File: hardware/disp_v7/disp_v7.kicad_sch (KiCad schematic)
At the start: 109 parts, among them J1 Conn_02x16_Odd_Even, Q1 2N7002, Q10 2N7002, Q11 2N7002, Q2 2N7002, Q3 2N7002, Q4 2N7002, Q5 2N7002, Q6 2N7002, Q7 2N7002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

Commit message: update version on disp to v7
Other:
- title: Disp V6 -> Disp

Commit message: main counter counting
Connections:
- net AUX_GPS_PPS: no longer names the net of J1.31 (Pin_31)
- net BOOT0: no longer names the net of R2.2
- net BOOT0: no longer J1.29 (Pin_29)
- net BOOT1: no longer names the net of J1.21 (Pin_21)
- net BOOT1: no longer R1.2
- net GPS_PPS: no longer names the net of J1.32 (Pin_32)
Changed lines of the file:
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@@
-    (effects (font (size 1.27 1.27)) (justify left bottom))
-  )
-  (label "BOOT0" (at 33.02 59.69 180) (fields_autoplaced)
-    (effects (font (size 1.27 1.27)) (justify right bottom))
-  )
-  (label "BOOT0" (at 171.45 25.4 0) (fields_autoplaced)
     (effects (font (size 1.27 1.27)) (justify left bottom))
   )
@@
     (effects (font (size 1.27 1.27)) (justify left bottom))
   )
-  (label "BOOT1" (at 171.45 36.83 0) (fields_autoplaced)
-    (effects (font (size 1.27 1.27)) (justify left bottom))
-  )
-  (label "BOOT1" (at 26.67 49.53 0) (fields_autoplaced)
-    (effects (font (size 1.27 1.27)) (justify left bottom))
-  )
   (label "ROW4" (at 26.67 36.83 0) (fields_autoplaced)
     (effects (font (size 1.27 1.27)) (justify left bottom))
@@
   (label "LEDH" (at 48.26 140.97 0) (fields_autoplaced)
     (effects (font (size 1.27 1.27)) (justify left bottom))
-  )
-  (label "AUX_GPS_PPS" (at 33.02 62.23 180) (fields_autoplaced)
-    (effects (font (size 1.27 1.27)) (justify right bottom))
   )
   (label "ROW6" (at 48.26 46.99 0) (fields_autoplaced)
@@
     (effects (font (size 1.27 1.27)) (justify left bottom))
   )
-  (label "GPS_PPS" (at 45.72 62.23 0) (fields_autoplaced)
-    (effects (font (size 1.27 1.27)) (justify left bottom))
-  )

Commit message: add switches
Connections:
- net ROW10: now reaches R2.2
- net ROW10: now also J1.29 (Pin_29)
- net ROW9: now reaches J1.21 (Pin_21)
- net ROW9: now also R1.2
- no-connect marks 0 -> 2
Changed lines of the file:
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@@
   (junction (at 88.9 148.59) (diameter 0) (color 0 0 0 0)
   )
+  (no_connect (at 45.72 62.23))
+  (no_connect (at 33.02 62.23))
   (wire (pts (xy 44.45 81.28) (xy 55.88 81.28))
     (stroke (width 0) (type default))
@@
     (effects (font (size 1.27 1.27)) (justify left bottom))
   )
+  (label "ROW9" (at 26.67 49.53 0) (fields_autoplaced)
+    (effects (font (size 1.27 1.27)) (justify left bottom))
+  )
   (label "ROW4" (at 26.67 36.83 0) (fields_autoplaced)
     (effects (font (size 1.27 1.27)) (justify left bottom))
@@
     (effects (font (size 1.27 1.27)) (justify left bottom))
   )
+  (label "ROW9" (at 171.45 36.83 0) (fields_autoplaced)
+    (effects (font (size 1.27 1.27)) (justify left bottom))
+  )
   (label "R6" (at 187.96 77.47 0) (fields_autoplaced)
     (effects (font (size 1.27 1.27)) (justify left bottom))
@@
     (effects (font (size 1.27 1.27)) (justify left bottom))
   )
+  (label "ROW10" (at 33.02 59.69 180) (fields_autoplaced)
+    (effects (font (size 1.27 1.27)) (justify right bottom))
+  )
   (label "ROW8" (at 48.26 49.53 0) (fields_autoplaced)
     (effects (font (size 1.27 1.27)) (justify left bottom))
@@
     (effects (font (size 1.27 1.27)) (justify left bottom))
   )
+  (label "ROW10" (at 171.45 25.4 0) (fields_autoplaced)
+    (effects (font (size 1.27 1.27)) (justify left bottom))
+  )

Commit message: clean up values
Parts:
- C32, C36, C38: value 100nF -> 100n
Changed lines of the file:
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@@
       (effects (font (size 1.27 1.27)) (justify left))
     )
-    (property "Value" "100nF" (at 58.42 87.6363 0)
+    (property "Value" "100n" (at 58.42 87.6363 0)
       (effects (font (size 1.27 1.27)) (justify left))
     )
@@
       (effects (font (size 1.27 1.27)))
     )
-    (property "Value" "4K7" (at 110.49 193.04 90)
+    (property "Value" "4K7" (at 105.41 193.04 90)
       (effects (font (size 1.27 1.27)))
     )
@@
       (effects (font (size 1.27 1.27)))
     )
-    (property "Value" "4K7" (at 82.55 144.78 90)
+    (property "Value" "4K7" (at 77.47 144.78 90)
       (effects (font (size 1.27 1.27)))
     )
@@
       (effects (font (size 1.27 1.27)))
     )
-    (property "Value" "4K7" (at 55.88 144.78 90)
+    (property "Value" "4K7" (at 50.8 144.78 90)
       (effects (font (size 1.27 1.27)))
     )
@@
       (effects (font (size 1.27 1.27)))
     )
-    (property "Value" "4K7" (at 25.4 144.78 90)
+    (property "Value" "4K7" (at 20.32 144.78 90)
       (effects (font (size 1.27 1.27)))
     )
@@
       (effects (font (size 1.27 1.27)))
     )
-    (property "Value" "4K7" (at 24.13 195.58 90)
+    (property "Value" "4K7" (at 19.05 195.58 90)
       (effects (font (size 1.27 1.27)))
     )
@@
       (effects (font (size 1.27 1.27)))
     )
-    (property "Value" "4K7" (at 111.76 146.05 90)
+    (property "Value" "4K7" (at 106.68 146.05 90)
       (effects (font (size 1.27 1.27)))
     )
@@
       (effects (font (size 1.27 1.27)))
     )
-    (property "Value" "4K7" (at 81.28 193.04 90)
+    (property "Value" "4K7" (at 76.2 193.04 90)
       (effects (font (size 1.27 1.27)))
     )
@@
       (effects (font (size 1.27 1.27)) (justify left))
     )
-    (property "Value" "100nF" (at 72.39 86.3663 0)
+    (property "Value" "100n" (at 72.39 86.3663 0)
       (effects (font (size 1.27 1.27)) (justify left))
     )
@@
       (effects (font (size 1.27 1.27)) (justify left))
     )
-    (property "Value" "100nF" (at 46.99 87.6363 0)
+    (property "Value" "100n" (at 46.99 87.6363 0)
       (effects (font (size 1.27 1.27)) (justify left))
     )
@@
       (effects (font (size 1.27 1.27)))
     )
-    (property "Value" "4K7" (at 57.15 193.04 90)
-      (effects (font (size 1.27 1.27)))
-    )
+    (property "Value" "4K7" (at 52.07 193.04 90)
+      (effects (font (size 1.27 1.27)))
+    )

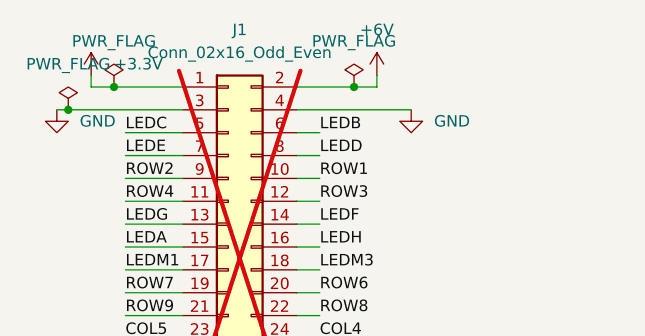
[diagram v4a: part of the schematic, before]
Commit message: fix up flip connector warning
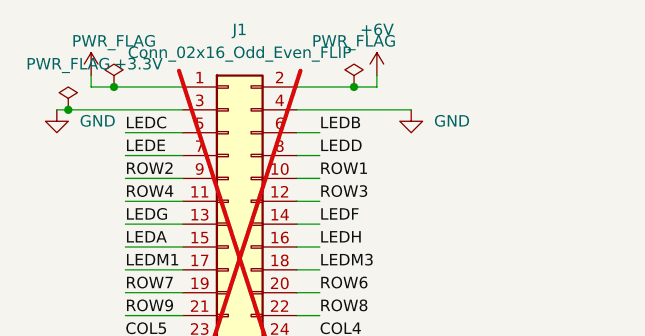
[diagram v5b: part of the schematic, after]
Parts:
- J1: value Conn_02x16_Odd_Even -> Conn_02x16_Odd_Even_FLIP; footprint Connector_PinHeader_2.54mm:PinHeader_2x16_P2.54mm_Vertical -> blinky_footprints:PinSocket_2x16_P2.54mm_Vertical_FLIP
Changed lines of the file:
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@@
       (effects (font (size 1.27 1.27)))
     )
-    (property "Value" "Conn_02x16_Odd_Even" (at 39.37 20.32 0)
+    (property "Value" "Conn_02x16_Odd_Even_FLIP" (at 39.37 20.32 0)
       (effects (font (size 1.27 1.27)))
     )
-    (property "Footprint" "Connector_PinHeader_2.54mm:PinHeader_2x16_P2.54mm_Vertical" (at 38.1 41.91 0)
+    (property "Footprint" "blinky_footprints:PinSocket_2x16_P2.54mm_Vertical_FLIP" (at 38.1 41.91 0)
       (effects (font (size 1.27 1.27)) hide)
     )
